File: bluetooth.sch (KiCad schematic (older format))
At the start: 55 parts, among them P100 LIPO, P110 CONN_1, P111 CONN_1, P112 CONN_1, P113 CONN_1, P114 CONN_1, P115 CONN_1, Q1 Nch, Q10 Nch, Q3 Nch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

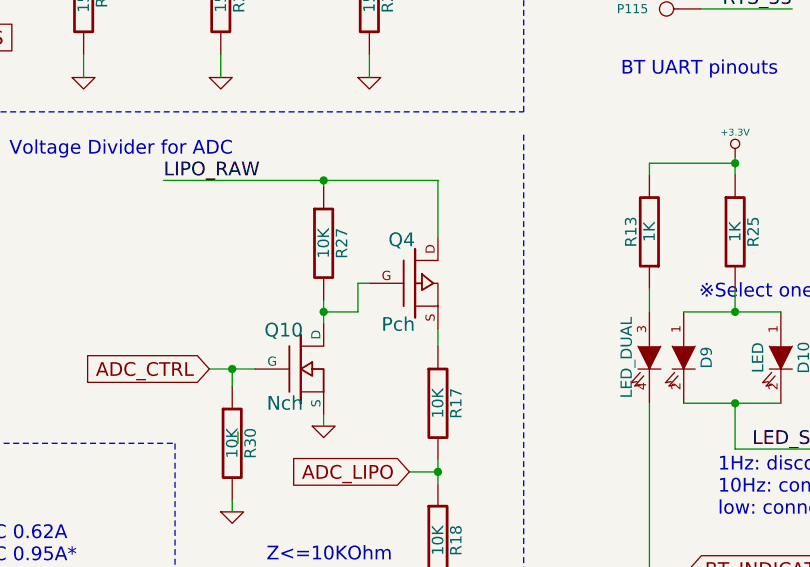
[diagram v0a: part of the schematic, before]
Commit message: Fix Q4 P-ch FET of ADC; exchange Drain and Source
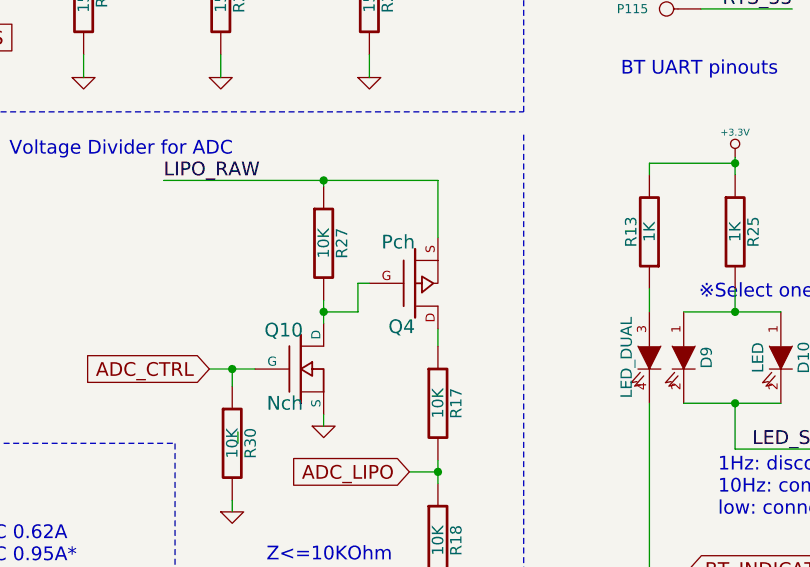
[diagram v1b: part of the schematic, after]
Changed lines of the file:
@@
 F 3 "" H 6100 2950 60  0000 C CNN
 	1    6100 2950
-	1    0    0    -1
+	1    0    0    1
 $EndComp
 $Comp

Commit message: Remove D5
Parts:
- removed D5: Schottky diode, keyboard_parts:D_SOD123, symbol DIODESCH
- U4: value MCP73831 -> MCP73832
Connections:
- wire segments 158 -> 157
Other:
- note added: "NOTE: Use 73832. 73831 leaks from VCC\nwhen no USB power"
- note removed: "block leak current from VCC\nwhen not charging"
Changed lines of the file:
@@
 P 5525 6625
 F 0 "U4" H 5525 6425 60  0000 C CNN
-F 1 "MCP73831" H 5525 6825 60  0000 C CNN
+F 1 "MCP73832" H 5525 6825 60  0000 C CNN
 F 2 "keyboard_parts:SOT23-5_HSOL" H 5525 6625 60  0001 C CNN
 F 3 "" H 5525 6625 60  0000 C CNN
@@
 Text Notes 6550 7475 2    60   ~ 0
 Charge current: Ichg = 1000V/Rprog
-Text Notes 6000 6475 0    60   ~ 0
-block leak current from VCC\nwhen not charging
 Text Notes 750  4250 0    60   ~ 0
 5V Output
@@
 Text Notes 7550 4850 0    60   ~ 0
 Power Indicator
-Text Label 5500 6175 0    60   ~ 0
+Text Label 5900 6350 0    60   ~ 0
 VUSB_IN
 $Comp
@@
 Text Notes 5450 4175 0    60   ~ 0
 Z<=10KOhm
-$Comp
-L PWR_FLAG #FLG056
-U 1 1 541843B8
-P 6475 6150
-F 0 "#FLG056" H 6475 6245 30  0001 C CNN
-F 1 "PWR_FLAG" H 6475 6330 30  0000 C CNN
-F 2 "" H 6475 6150 60  0000 C CNN
-F 3 "" H 6475 6150 60  0000 C CNN
-	1    6475 6150
-	1    0    0    -1
-$EndComp
-$Comp
-L DIODESCH D5
-U 1 1 545237C3
-P 6125 6175
-F 0 "D5" H 6125 6275 40  0000 C CNN
-F 1 "Schottky diode" H 6125 6075 40  0000 C CNN
-F 2 "keyboard_parts:D_SOD123" H 6125 6175 60  0001 C CNN
-F 3 "" H 6125 6175 60  0000 C CNN
-	1    6125 6175
-	1    0    0    -1
-$EndComp
 Text Notes 2600 3300 0    60   ~ 0
 Optional\nFor TAR5SB33
@@
 X5R
 $Comp
-L GND #PWR057
+L GND #PWR056
 U 1 1 51BE968F
 P 6200 4375
-F 0 "#PWR057" H 6200 4375 30  0001 C CNN
+F 0 "#PWR056" H 6200 4375 30  0001 C CNN
 F 1 "GND" H 6200 4305 30  0001 C CNN
 F 2 "" H 6200 4375 60  0000 C CNN
@@
 $EndComp
 $Comp
-L GND #PWR058
+L GND #PWR057
 U 1 1 5452B28D
 P 5700 3575
-F 0 "#PWR058" H 5700 3575 30  0001 C CNN
+F 0 "#PWR057" H 5700 3575 30  0001 C CNN
 F 1 "GND" H 5700 3505 30  0001 C CNN
 F 2 "" H 5700 3575 60  0000 C CNN
@@
 Connection ~ 6475 6525
 Wire Wire Line
-	6475 6150 6475 6825
+	6475 6350 6475 6825
 Wire Wire Line
 	4525 6175 4525 6825
@@
 	2475 1875 3125 1875
 Wire Wire Line
-	1200 1875 600  1875
-Wire Wire Line
-	2000 1875 1600 1875
-Wire Wire Line
-	3925 1875 3525 1875
+	600  1875 1200 1875
+Wire Wire Line
+	1600 1875 2000 1875
+Wire Wire Line
+	3525 1875 3925 1875
 Wire Wire Line
 	5250 700  5300 700
@@
 	8075 6150 8475 6150
 Wire Wire Line
-	8475 5750 8075 5750
+	8075 5750 8475 5750
 Wire Wire Line
 	8275 5100 8275 5175
@@
 	6200 4375 6200 4325
 Wire Wire Line
-	6475 6175 6325 6175
-Wire Wire Line
-	5925 6175 5500 6175
-Connection ~ 6475 6175
+	5900 6350 6475 6350
 Wire Wire Line
 	6200 3775 6075 3775
@@
 	4200 3650 675  3650
 Wire Wire Line
-	5400 3325 5200 3325
+	5200 3325 5400 3325
 Wire Wire Line
 	5300 3400 5300 3325
@@
 Wire Notes Line
 	5050 5600 5050 4525
+Text Notes 4300 7700 0    60   ~ 12
+NOTE: Use 73832. 73831 leaks from VCC\nwhen no USB power
 $EndSCHEMATC

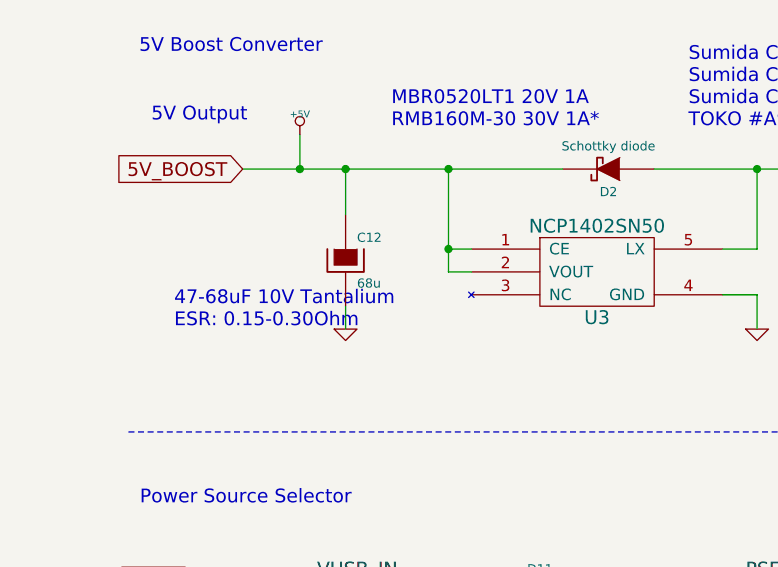
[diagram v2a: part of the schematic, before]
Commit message: Change value of C12; 68u to 47u
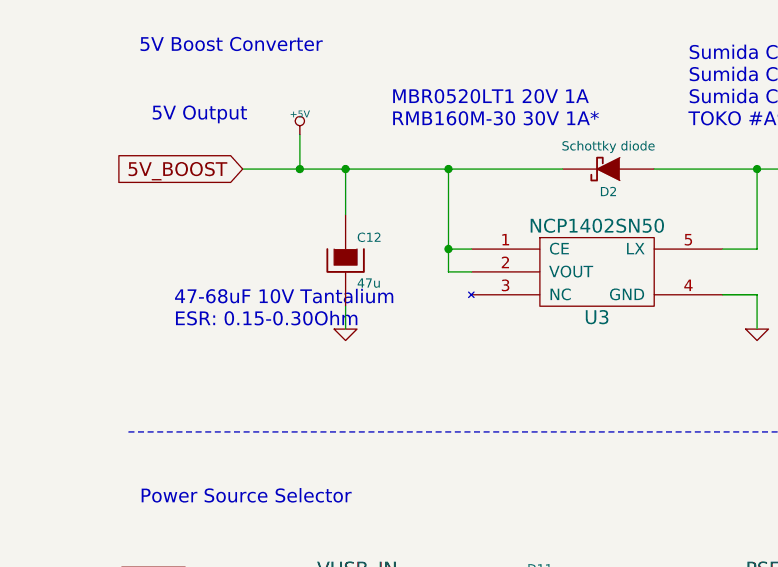
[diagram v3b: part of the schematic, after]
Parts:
- C12: value 68u -> 47u
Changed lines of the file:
@@
 P 1600 4850
 F 0 "C12" H 1650 4950 40  0000 L CNN
-F 1 "68u" H 1650 4750 40  0000 L CNN
+F 1 "47u" H 1650 4750 40  0000 L CNN
 F 2 "keyboard_parts:C_3528" H 1700 4700 30  0001 C CNN
 F 3 "" H 1600 4850 300 0000 C CNN

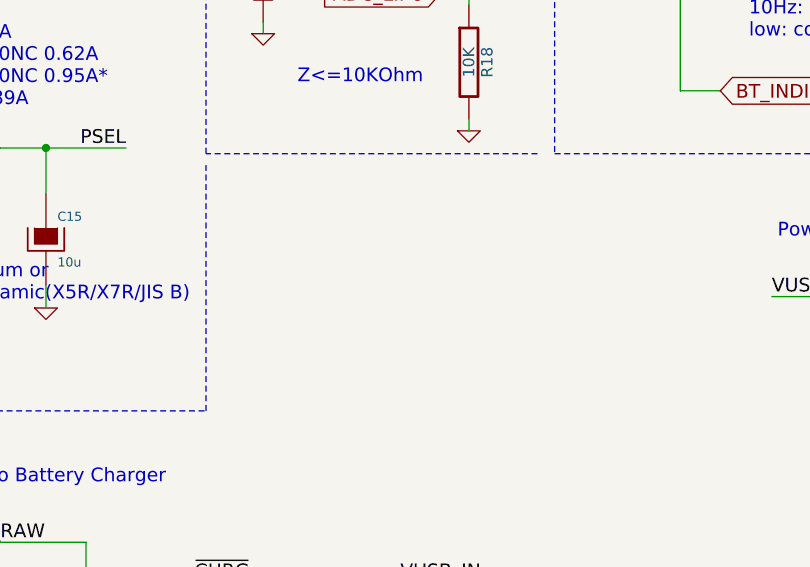
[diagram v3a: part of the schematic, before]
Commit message: Add current measure pins and change pin pad size
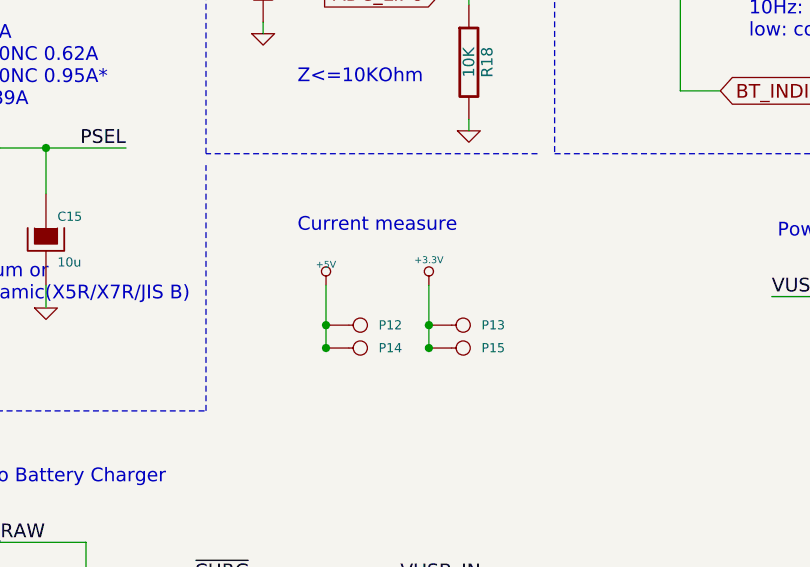
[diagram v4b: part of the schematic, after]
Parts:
- added P12, P13, P14, P15: CONN_1, keyboard_parts:PIN_1, symbol CONN_1
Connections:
- wire segments 157 -> 159
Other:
- note added: "Current measure"
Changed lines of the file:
@@
 L +3.3V #PWR037
 U 1 1 51B8A63B
-P 7850 950
-F 0 "#PWR037" H 7850 910 30  0001 C CNN
-F 1 "+3.3V" H 7850 1060 30  0000 C CNN
-F 2 "" H 7850 950 60  0000 C CNN
-F 3 "" H 7850 950 60  0000 C CNN
-	1    7850 950
+P 6025 5050
+F 0 "#PWR037" H 6025 5010 30  0001 C CNN
+F 1 "+3.3V" H 6025 5160 30  0000 C CNN
+F 2 "" H 6025 5050 60  0000 C CNN
+F 3 "" H 6025 5050 60  0000 C CNN
+	1    6025 5050
 	1    0    0    -1
 $EndComp
@@
 	1    0    0    -1
 $EndComp
+Text Notes 4300 7700 0    60   ~ 12
+NOTE: Use 73832. 73831 leaks from VCC\nwhen no USB power
+$Comp
+L CONN_1 P15
+U 1 1 54862C03
+P 6175 5325
+F 0 "P15" H 6255 5325 40  0000 L CNN
+F 1 "CONN_1" H 6175 5380 30  0001 C CNN
+F 2 "keyboard_parts:PIN_1" H 6175 5325 60  0001 C CNN
+F 3 "" H 6175 5325 60  0000 C CNN
+	1    6175 5325
+	1    0    0    -1
+$EndComp
+$Comp
+L CONN_1 P13
+U 1 1 54862C9E
+P 6175 5225
+F 0 "P13" H 6255 5225 40  0000 L CNN
+F 1 "CONN_1" H 6175 5280 30  0001 C CNN
+F 2 "keyboard_parts:PIN_1" H 6175 5225 60  0001 C CNN
+F 3 "" H 6175 5225 60  0000 C CNN
+	1    6175 5225
+	1    0    0    -1
+$EndComp
 Wire Notes Line
 	6575 2200 6575 575
@@
 	675  2200 6575 2200
 Wire Wire Line
-	7850 1000 7850 950
+	6025 5050 6025 5325
 Wire Wire Line
 	7850 1450 7850 1550
@@
 Wire Notes Line
 	5050 5600 5050 4525
-Text Notes 4300 7700 0    60   ~ 12
-NOTE: Use 73832. 73831 leaks from VCC\nwhen no USB power
+Connection ~ 6025 5325
+Connection ~ 6025 5225
+$Comp
+L +5V #PWR058
+U 1 1 5486405C
+P 5575 5050
+F 0 "#PWR058" H 5575 5140 20  0001 C CNN
+F 1 "+5V" H 5575 5140 30  0000 C CNN
+F 2 "" H 5575 5050 60  0000 C CNN
+F 3 "" H 5575 5050 60  0000 C CNN
+	1    5575 5050
+	1    0    0    -1
+$EndComp
+Wire Wire Line
+	5575 5050 5575 5325
+$Comp
+L CONN_1 P14
+U 1 1 54864365
+P 5725 5325
+F 0 "P14" H 5805 5325 40  0000 L CNN
+F 1 "CONN_1" H 5725 5380 30  0001 C CNN
+F 2 "keyboard_parts:PIN_1" H 5725 5325 60  0001 C CNN
+F 3 "" H 5725 5325 60  0000 C CNN
+	1    5725 5325
+	1    0    0    -1
+$EndComp
+$Comp
+L CONN_1 P12
+U 1 1 5486436B
+P 5725 5225
+F 0 "P12" H 5805 5225 40  0000 L CNN
+F 1 "CONN_1" H 5725 5280 30  0001 C CNN
+F 2 "keyboard_parts:PIN_1" H 5725 5225 60  0001 C CNN
+F 3 "" H 5725 5225 60  0000 C CNN
+	1    5725 5225
+	1    0    0    -1
+$EndComp
+Connection ~ 5575 5325
+Connection ~ 5575 5225
+Text Notes 5450 4825 0    60   ~ 0
+Current measure
+$Comp
+L +3.3V #PWR059
+U 1 1 54867546
+P 7850 950
+F 0 "#PWR059" H 7850 910 30  0001 C CNN
+F 1 "+3.3V" H 7850 1060 30  0000 C CNN
+F 2 "" H 7850 950 60  0000 C CNN
+F 3 "" H 7850 950 60  0000 C CNN
+	1    7850 950
+	1    0    0    -1
+$EndComp
+Wire Wire Line
+	7850 1000 7850 950
 $EndSCHEMATC

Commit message: Fix sw board connector for Pro
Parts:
- D10, D4: footprint keyboard_parts:LED_TH -> keyboard_parts:LED_TH_BIVAR
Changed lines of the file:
@@
 Sheet 2 2
 Title "HHKB Alt Controller"
-Date "2015/03"
-Rev "G"
+Date "2015/05"
+Rev "Hp"
 Comp "TMK"
 Comment1 ""
@@
 F 0 "D4" H 8475 6050 50  0000 C CNN
 F 1 "LED" H 8475 5850 50  0000 C CNN
-F 2 "keyboard_parts:LED_TH" H 8475 5950 60  0001 C CNN
+F 2 "keyboard_parts:LED_TH_BIVAR" H 8475 5950 60  0001 C CNN
 F 3 "" H 8475 5950 60  0000 C CNN
 	1    8475 5950
@@
 F 0 "D10" H 7700 3375 50  0000 C CNN
 F 1 "LED" H 7700 3175 50  0000 C CNN
-F 2 "keyboard_parts:LED_TH" H 7700 3275 60  0001 C CNN
+F 2 "keyboard_parts:LED_TH_BIVAR" H 7700 3275 60  0001 C CNN
 F 3 "" H 7700 3275 60  0000 C CNN
 	1    7700 3275
